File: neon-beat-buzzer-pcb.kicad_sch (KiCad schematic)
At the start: 66 parts, among them J1 BATT_CON, J2 SWITCH_CON, J3 BUTTON_CON, J4 USB_C_Receptacle_USB2.0_16P, U1 ESP32-C3-MINI-1, U2 BQ24074RGT, U3 TPS22929D, U4 74AHCT1G125, U5 TPS610997DRV, U6 USBLC6-2SC6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

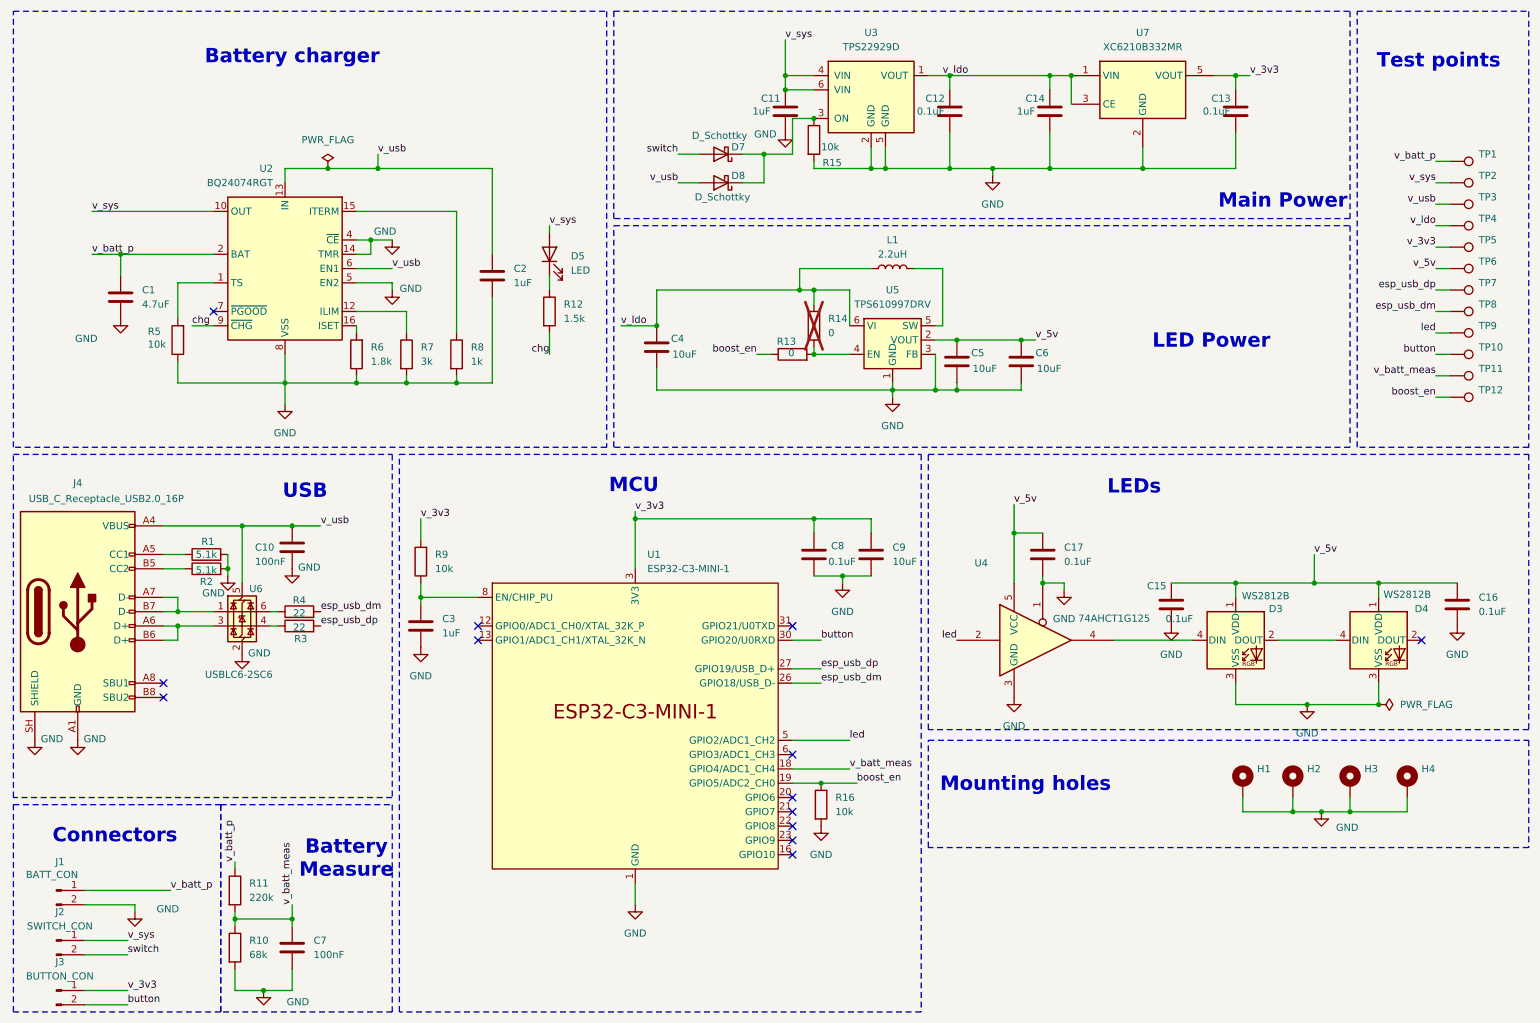
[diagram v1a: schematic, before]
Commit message: board: fix layout
Move the boost input from v_sys to v_ldo. Update the PCB accordingly.
While at it, import JLCPCB design rules. There are still a lot of
silkscreen clearance issues to fix.

Signed-off-by: Alexis Lothoré <alexis.lothore@gmail.com>
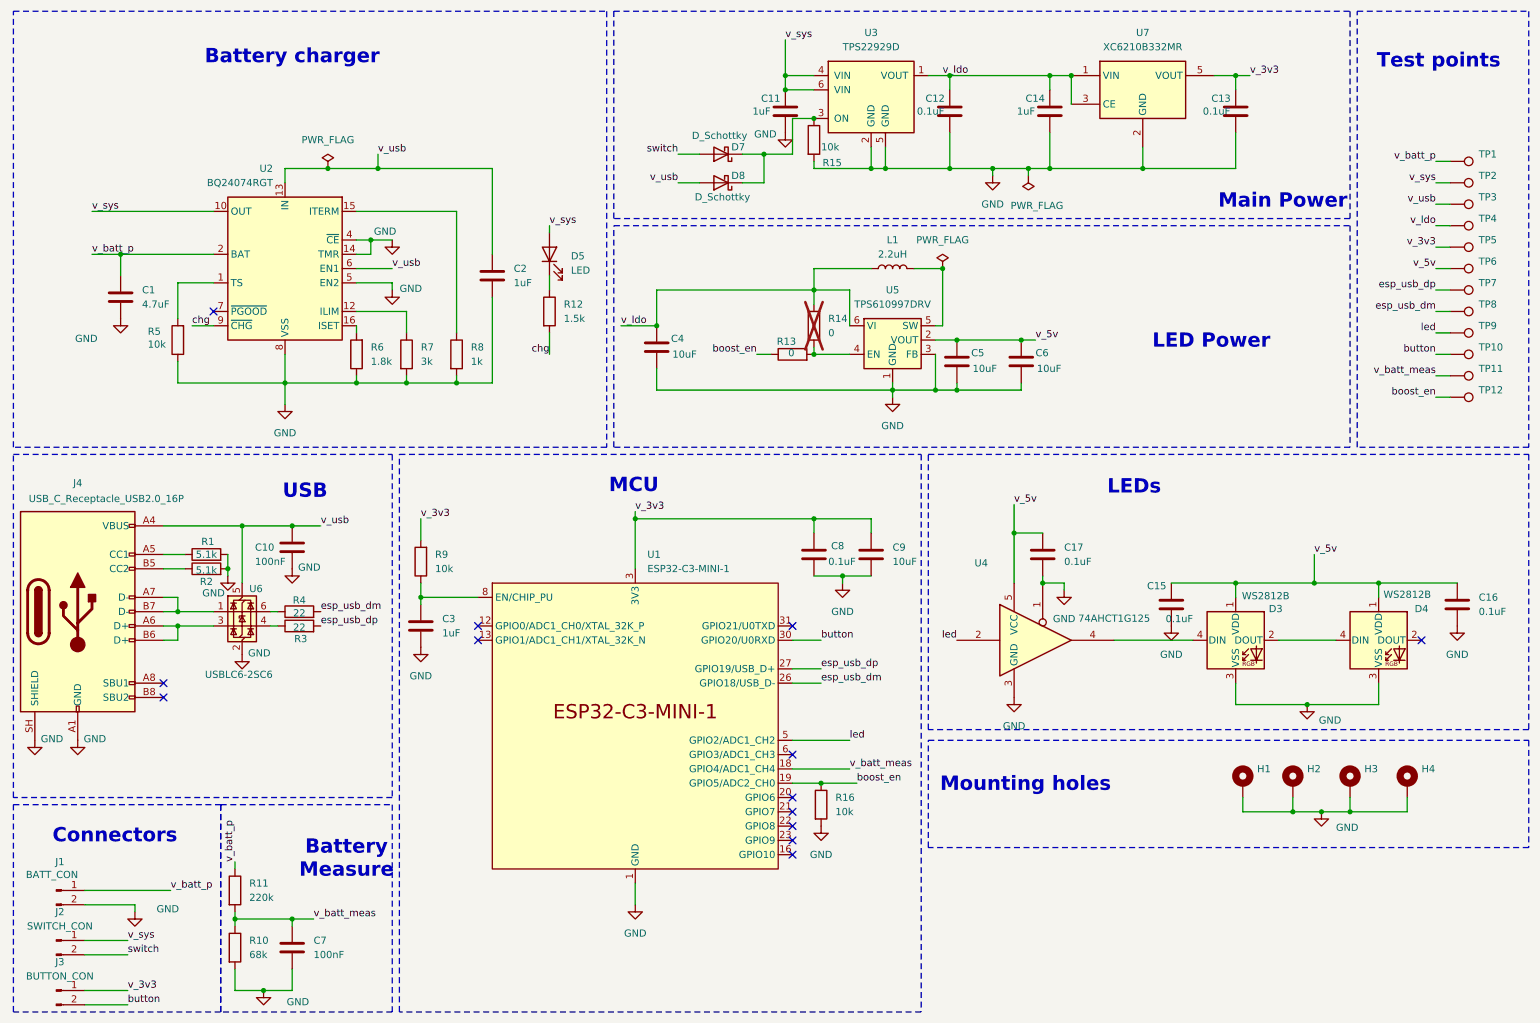
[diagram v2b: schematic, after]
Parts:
- J1, J2, J3: footprint Connector_Molex:Molex_PicoBlade_53048-0210_1x02_P1.25mm_Horizontal -> Connector_Molex:Molex_PicoBlade_53261-0271_1x02-1MP_P1.25mm_Horizontal
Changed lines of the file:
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@@
 	)
 	(junction
+		(at 179.07 59.69)
+		(diameter 0)
+		(color 0 0 0 0)
+	)
+	(junction
 		(at 156.21 74.93)
 		(diameter 0)
@@
 	)
 	(junction
+		(at 194.31 41.91)
+		(diameter 0)
+		(color 0 0 0 0)
+	)
+	(junction
 		(at 58.42 187.96)
 		(diameter 0)
@@
 	)
 	(junction
-		(at 256.54 137.16)
-		(diameter 0)
-		(color 0 0 0 0)
-	)
-	(junction
-		(at 63.5 175.26)
-		(diameter 0)
-		(color 0 0 0 0)
-	)
-	(junction
 		(at 231.14 115.57)
 		(diameter 0)
@@
 	)
 	(junction
+		(at 63.5 175.26)
+		(diameter 0)
+		(color 0 0 0 0)
+	)
+	(junction
 		(at 177.8 81.28)
 		(diameter 0)
@@
 	)
 	(junction
-		(at 153.67 63.5)
-		(diameter 0)
-		(color 0 0 0 0)
-	)
-	(junction
 		(at 69.85 41.91)
 		(diameter 0)
@@
 	(wire
 		(pts
-			(xy 63.5 172.72) (xy 63.5 175.26)
+			(xy 200.66 115.57) (xy 200.66 116.84)
 		)
 		(stroke
@@
 	(wire
 		(pts
-			(xy 200.66 115.57) (xy 200.66 116.84)
+			(xy 179.07 59.69) (xy 179.07 69.85)
 		)
 		(stroke
@@
 	(wire
 		(pts
-			(xy 179.07 59.69) (xy 179.07 69.85)
+			(xy 147.32 44.45) (xy 147.32 39.37)
 		)
 		(stroke
@@
 	(wire
 		(pts
-			(xy 147.32 44.45) (xy 147.32 39.37)
+			(xy 63.5 184.15) (xy 63.5 187.96)
 		)
 		(stroke
@@
 	(wire
 		(pts
-			(xy 63.5 184.15) (xy 63.5 187.96)
+			(xy 256.54 137.16) (xy 256.54 133.35)
 		)
 		(stroke
@@
 	(wire
 		(pts
-			(xy 256.54 137.16) (xy 256.54 133.35)
+			(xy 62.23 41.91) (xy 62.23 44.45)
 		)
 		(stroke
@@
 	(wire
 		(pts
-			(xy 62.23 41.91) (xy 62.23 44.45)
+			(xy 86.36 104.14) (xy 86.36 107.95)
 		)
 		(stroke
@@
 	(wire
 		(pts
-			(xy 86.36 104.14) (xy 86.36 107.95)
+			(xy 67.31 175.26) (xy 63.5 175.26)
 		)
 		(stroke
@@
 	(wire
 		(pts
+			(xy 194.31 43.18) (xy 194.31 41.91)
+		)
+		(stroke
+			(width 0)
+			(type default)
+		)
+	)
+	(wire
+		(pts
 			(xy 198.12 25.4) (xy 201.93 25.4)
 		)
@@
 	(wire
 		(pts
-			(xy 166.37 59.69) (xy 153.67 59.69)
+			(xy 166.37 59.69) (xy 156.21 59.69)
 		)
 		(stroke
@@
 	(wire
 		(pts
-			(xy 153.67 63.5) (xy 156.21 63.5)
-		)
-		(stroke
-			(width 0)
-			(type default)
-		)
-	)
-	(wire
-		(pts
 			(xy 166.37 41.91) (xy 166.37 38.1)
 		)
@@
 	(wire
 		(pts
-			(xy 128.27 63.5) (xy 153.67 63.5)
+			(xy 128.27 63.5) (xy 156.21 63.5)
 		)
 		(stroke
@@
 	(wire
 		(pts
-			(xy 153.67 59.69) (xy 153.67 63.5)
+			(xy 156.21 59.69) (xy 156.21 63.5)
 		)
 		(stroke
@@
 	(wire
 		(pts
+			(xy 194.31 41.91) (xy 198.12 41.91)
+		)
+		(stroke
+			(width 0)
+			(type default)
+		)
+	)
+	(wire
+		(pts
 			(xy 77.47 57.15) (xy 77.47 54.61)
 		)
@@
 	(wire
 		(pts
-			(xy 187.96 41.91) (xy 198.12 41.91)
+			(xy 187.96 41.91) (xy 194.31 41.91)
 		)
 		(stroke
@@
 	)
 	(label "v_batt_meas"
-		(at 63.5 172.72 90)
+		(at 67.31 175.26 0)
 		(effects
 			(font
@@
 	)
 	(symbol
-		(lib_id "power:PWR_FLAG")
-		(at 256.54 137.16 270)
-		(unit 1)
-		(body_style 1)
-		(exclude_from_sim no)
-		(in_bom yes)
-		(on_board yes)
-		(in_pos_files yes)
-		(dnp no)
-		(fields_autoplaced yes)
-		(property "Reference" "#FLG01"
-			(at 258.445 137.16 0)
-			(hide yes)
-			(show_name no)
-			(do_not_autoplace no)
-			(effects
-				(font
-					(size 1.27 1.27)
-				)
-			)
-		)
-		(property "Value" "PWR_FLAG"
-			(at 260.35 137.1599 90)
-			(show_name no)
-			(do_not_autoplace no)
-			(effects
-				(font
-					(size 1.27 1.27)
-				)
-				(justify left)
-			)
-		)
-		(property "Footprint" ""
-			(at 256.54 137.16 0)
-			(hide yes)
-			(show_name no)
-			(do_not_autoplace no)
-			(effects
-				(font
-					(size 1.27 1.27)
-				)
-			)
-		)
-		(property "Datasheet" ""
-			(at 256.54 137.16 0)
-			(hide yes)
-			(show_name no)
-			(do_not_autoplace no)
-			(effects
-				(font
-					(size 1.27 1.27)
-				)
-			)
-		)
-		(property "Description" "Special symbol for telling ERC where power comes from"
-			(at 256.54 137.16 0)
-			(hide yes)
-			(show_name no)
-			(do_not_autoplace no)
-			(effects
-				(font
-					(size 1.27 1.27)
-				)
-			)
-		)
-		(pin "1"
-		)
-		(instances
-			(project "neon-beat-buzzer-pcb"
-				(path "/1aa5bb6d-1502-4465-bf5e-41cf5ab51d4a"
-					(reference "#FLG01")
-					(unit 1)
-				)
-			)
-		)
-	)
-	(symbol
 		(lib_id "Device:C")
 		(at 231.14 31.75 0)
@@
 			)
 		)
-		(property "Footprint" "Connector_Molex:Molex_PicoBlade_53048-0210_1x02_P1.25mm_Horizontal"
+		(property "Footprint" "Connector_Molex:Molex_PicoBlade_53261-0271_1x02-1MP_P1.25mm_Horizontal"
 			(at 21.59 187.96 0)
 			(hide yes)
@@
 	)
 	(symbol
+		(lib_id "power:PWR_FLAG")
+		(at 194.31 43.18 180)
+		(unit 1)
+		(body_style 1)
+		(exclude_from_sim no)
+		(in_bom yes)
+		(on_board yes)
+		(in_pos_files yes)
+		(dnp no)
+		(property "Reference" "#FLG01"
+			(at 194.31 45.085 0)
+			(hide yes)
+			(show_name no)
+			(do_not_autoplace no)
+			(effects
+				(font
+					(size 1.27 1.27)
+				)
+			)
+		)
+		(property "Value" "PWR_FLAG"
+			(at 195.834 48.514 0)
+			(show_name no)
+			(do_not_autoplace no)
+			(effects
+				(font
+					(size 1.27 1.27)
+				)
+			)
+		)
+		(property "Footprint" ""
+			(at 194.31 43.18 0)
+			(hide yes)
+			(show_name no)
+			(do_not_autoplace no)
+			(effects
+				(font
+					(size 1.27 1.27)
+				)
+			)
+		)
+		(property "Datasheet" ""
+			(at 194.31 43.18 0)
+			(hide yes)
+			(show_name no)
+			(do_not_autoplace no)
+			(effects
+				(font
+					(size 1.27 1.27)
+				)
+			)
+		)
+		(property "Description" "Special symbol for telling ERC where power comes from"
+			(at 194.31 43.18 0)
+			(hide yes)
+			(show_name no)
+			(do_not_autoplace no)
+			(effects
+				(font
+					(size 1.27 1.27)
+				)
+			)
+		)
+		(pin "1"
+		)
+		(instances
+			(project "neon-beat-buzzer-pcb"
+				(path "/1aa5bb6d-1502-4465-bf5e-41cf5ab51d4a"
+					(reference "#FLG01")
+					(unit 1)
+				)
+			)
+		)
+	)
+	(symbol
 		(lib_id "power:GND")
 		(at 187.96 43.18 0)
@@
 			)
 		)
-		(property "Footprint" "Connector_Molex:Molex_PicoBlade_53048-0210_1x02_P1.25mm_Horizontal"
+		(property "Footprint" "Connector_Molex:Molex_PicoBlade_53261-0271_1x02-1MP_P1.25mm_Horizontal"
 			(at 21.59 179.07 0)
 			(hide yes)
@@
 	)
 	(symbol
+		(lib_id "power:PWR_FLAG")
+		(at 179.07 59.69 0)
+		(unit 1)
+		(body_style 1)
+		(exclude_from_sim no)
+		(in_bom yes)
+		(on_board yes)
+		(in_pos_files yes)
+		(dnp no)
+		(fields_autoplaced yes)
+		(property "Reference" "#FLG02"
+			(at 179.07 57.785 0)
+			(hide yes)
+			(show_name no)
+			(do_not_autoplace no)
+			(effects
+				(font
+					(size 1.27 1.27)
+				)
+			)
+		)
+		(property "Value" "PWR_FLAG"
+			(at 179.07 54.61 0)
+			(show_name no)
+			(do_not_autoplace no)
+			(effects
+				(font
+					(size 1.27 1.27)
+				)
+			)
+		)
+		(property "Footprint" ""
+			(at 179.07 59.69 0)
+			(hide yes)
+			(show_name no)
+			(do_not_autoplace no)
+			(effects
+				(font
+					(size 1.27 1.27)
+				)
+			)
+		)
+		(property "Datasheet" ""
+			(at 179.07 59.69 0)
+			(hide yes)
+			(show_name no)
+			(do_not_autoplace no)
+			(effects
+				(font
+					(size 1.27 1.27)
+				)
+			)
+		)
+		(property "Description" "Special symbol for telling ERC where power comes from"
+			(at 179.07 59.69 0)
+			(hide yes)
+			(show_name no)
+			(do_not_autoplace no)
+			(effects
+				(font
+					(size 1.27 1.27)
+				)
+			)
+		)
+		(pin "1"
+		)
+		(instances
+			(project "neon-beat-buzzer-pcb"
+				(path "/1aa5bb6d-1502-4465-bf5e-41cf5ab51d4a"
+					(reference "#FLG02")
+					(unit 1)
+				)
+			)
+		)
+	)
+	(symbol
 		(lib_id "power:GND")
 		(at 219.71 123.19 0)
@@
 		(in_pos_files yes)
 		(dnp no)
-		(fields_autoplaced yes)
 		(property "Reference" "#PWR011"
 			(at 243.84 143.51 0)
@@
 		)
 		(property "Value" "GND"
-			(at 243.84 142.24 0)
+			(at 247.904 139.954 0)
 			(show_name no)
 			(do_not_autoplace no)
@@
 			)
 		)
-		(property "Footprint" "Connector_Molex:Molex_PicoBlade_53048-0210_1x02_P1.25mm_Horizontal"
+		(property "Footprint" "Connector_Molex:Molex_PicoBlade_53261-0271_1x02-1MP_P1.25mm_Horizontal"
 			(at 21.59 170.18 0)
 			(hide yes)
